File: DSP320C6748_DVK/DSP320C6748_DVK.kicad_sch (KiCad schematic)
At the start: 0 parts

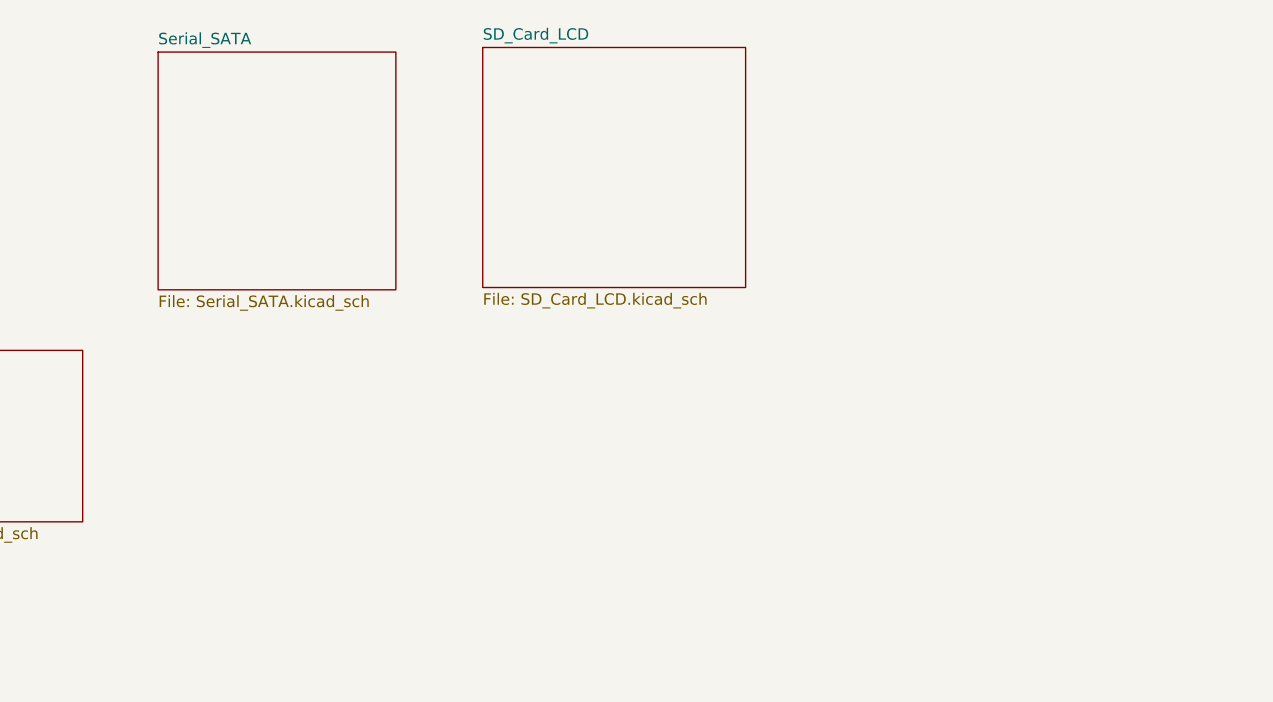
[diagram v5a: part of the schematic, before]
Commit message: DDR_RAM and Video Decoder Schematic Added
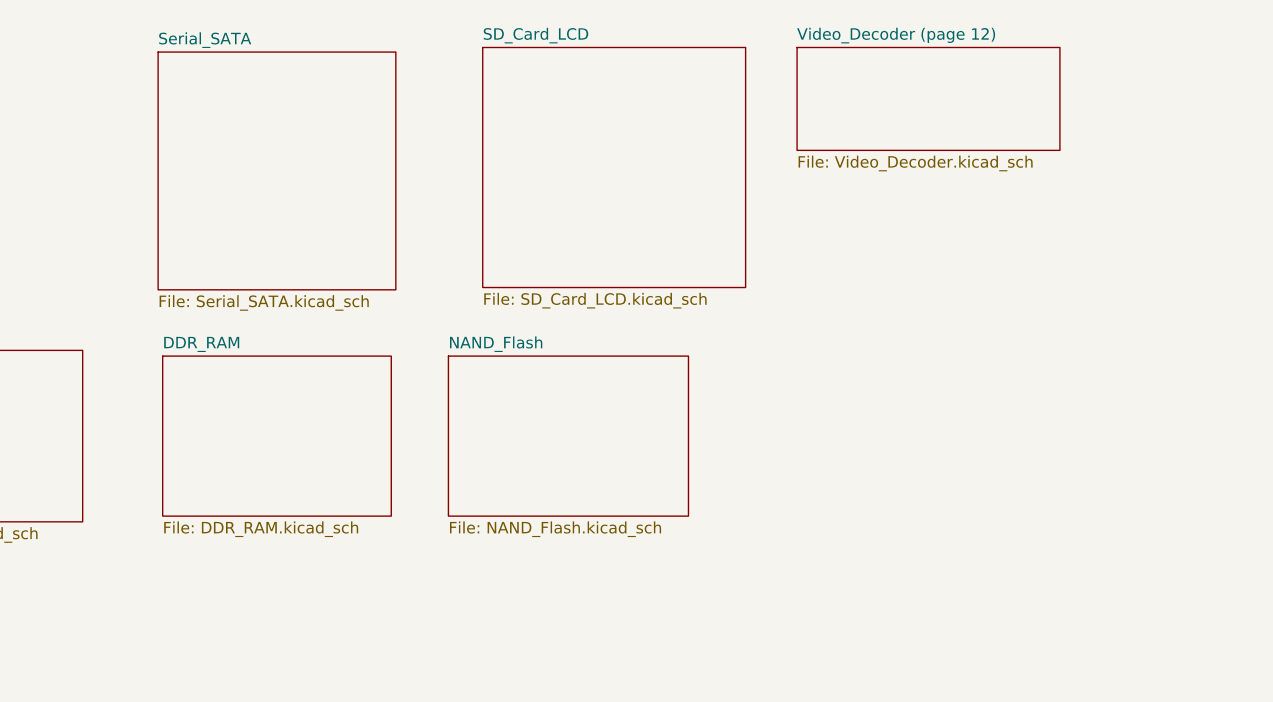
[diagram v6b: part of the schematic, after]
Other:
- added sheet DDR_RAM (DDR_RAM.kicad_sch)
- added sheet NAND_Flash (NAND_Flash.kicad_sch)
- added sheet Video_Decoder (page 12) (Video_Decoder.kicad_sch)
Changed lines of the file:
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@@
+	)
+	(sheet
+		(at 222.885 24.13)
+		(size 29.21 11.43)
+		(exclude_from_sim no)
+		(in_bom yes)
+		(on_board yes)
+		(dnp no)
+		(fields_autoplaced yes)
+		(stroke
+			(width 0.1524)
+			(type solid)
+		)
+		(fill
+			(color 0 0 0 0)
+		)
+		(property "Sheetname" "Video_Decoder (page 12)"
+			(at 222.885 23.4184 0)
+			(show_name no)
+			(do_not_autoplace no)
+			(effects
+				(font
+					(size 1.27 1.27)
+				)
+				(justify left bottom)
+			)
+		)
+		(property "Sheetfile" "Video_Decoder.kicad_sch"
+			(at 222.885 36.1446 0)
+			(show_name no)
+			(do_not_autoplace no)
+			(effects
+				(font
+					(size 1.27 1.27)
+				)
+				(justify left top)
+			)
+		)
+		(instances
+			(project "DSP320C6748_DVK"
+				(path "/3a70ffc0-9fe7-4a5b-b3c2-23140355df82"
+					(page "12")
+				)
+			)
+		)
 	)
 	(sheet
@@
 	)
 	(sheet
+		(at 152.4 58.42)
+		(size 25.4 17.78)
+		(exclude_from_sim no)
+		(in_bom yes)
+		(on_board yes)
+		(dnp no)
+		(fields_autoplaced yes)
+		(stroke
+			(width 0.1524)
+			(type solid)
+		)
+		(fill
+			(color 0 0 0 0)
+		)
+		(property "Sheetname" "DDR_RAM"
+			(at 152.4 57.7084 0)
+			(show_name no)
+			(do_not_autoplace no)
+			(effects
+				(font
+					(size 1.27 1.27)
+				)
+				(justify left bottom)
+			)
+		)
+		(property "Sheetfile" "DDR_RAM.kicad_sch"
+			(at 152.4 76.7846 0)
+			(show_name no)
+			(do_not_autoplace no)
+			(effects
+				(font
+					(size 1.27 1.27)
+				)
+				(justify left top)
+			)
+		)
+		(instances
+			(project "DSP320C6748_DVK"
+				(path "/3a70ffc0-9fe7-4a5b-b3c2-23140355df82"
+					(page "10")
+				)
+			)
+		)
+	)
+	(sheet
 		(at 120.015 57.785)
 		(size 23.495 19.05)
@@
 				)
 			)
+		)
+	)
+	(sheet
+		(at 184.15 58.42)
+		(size 26.67 17.78)
+		(exclude_from_sim no)
+		(in_bom yes)
+		(on_board yes)
+		(dnp no)
+		(fields_autoplaced yes)
+		(stroke
+			(width 0.1524)
+			(type solid)
+		)
+		(fill
+			(color 0 0 0 0)
+		)
+		(property "Sheetname" "NAND_Flash"
+			(at 184.15 57.7084 0)
+			(show_name no)
+			(do_not_autoplace no)
+			(effects
+				(font
+					(size 1.27 1.27)
+				)
+				(justify left bottom)
+			)
+		)
+		(property "Sheetfile" "NAND_Flash.kicad_sch"
+			(at 184.15 76.7846 0)
+			(show_name no)
+			(do_not_autoplace no)
+			(effects
+				(font
+					(size 1.27 1.27)
+				)
+				(justify left top)
+			)
+		)
+		(instances
+			(project "DSP320C6748_DVK"
+				(path "/3a70ffc0-9fe7-4a5b-b3c2-23140355df82"
+					(page "11")
+				)
+			)

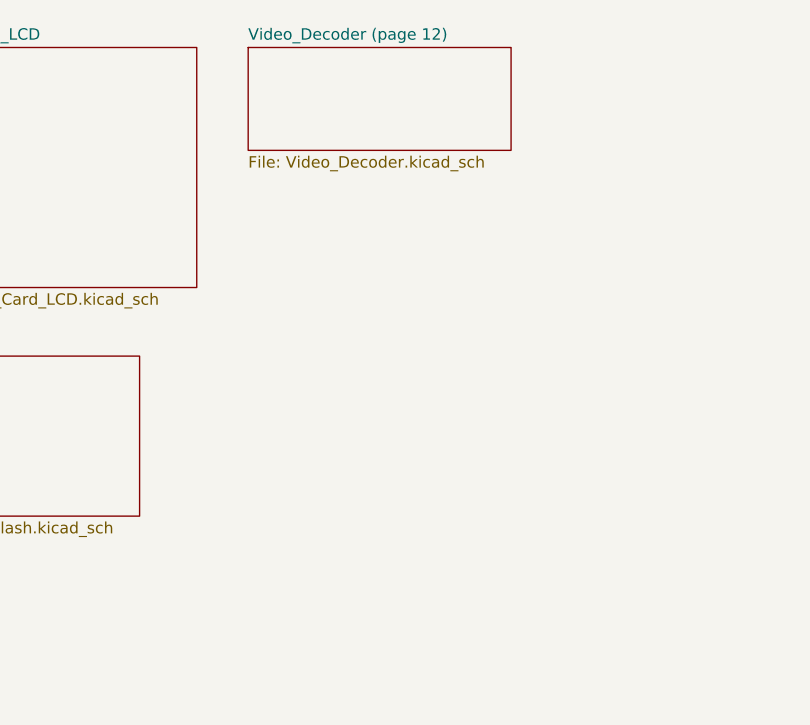
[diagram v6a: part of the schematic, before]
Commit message: Video and Audio Codec Schematic added
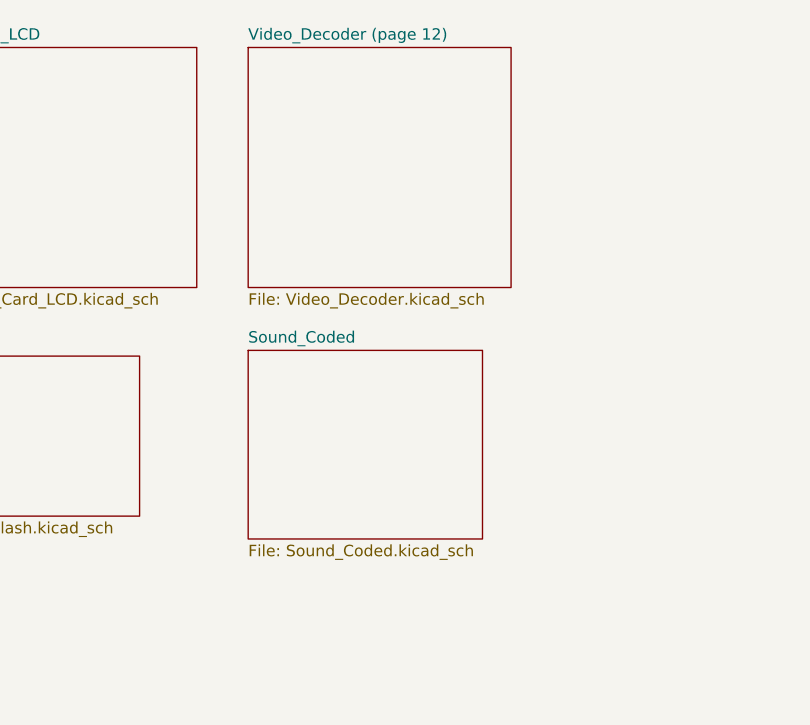
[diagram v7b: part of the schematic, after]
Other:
- added sheet Sound_Coded (Sound_Coded.kicad_sch)
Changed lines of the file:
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@@
 	(sheet
 		(at 222.885 24.13)
-		(size 29.21 11.43)
+		(size 29.21 26.67)
 		(exclude_from_sim no)
 		(in_bom yes)
@@
 		)
 		(property "Sheetfile" "Video_Decoder.kicad_sch"
-			(at 222.885 36.1446 0)
+			(at 222.885 51.3846 0)
 			(show_name no)
 			(do_not_autoplace no)
@@
 				)
 			)
+		)
+	)
+	(sheet
+		(at 222.885 57.785)
+		(size 26.035 20.955)
+		(exclude_from_sim no)
+		(in_bom yes)
+		(on_board yes)
+		(dnp no)
+		(fields_autoplaced yes)
+		(stroke
+			(width 0.1524)
+			(type solid)
+		)
+		(fill
+			(color 0 0 0 0)
+		)
+		(property "Sheetname" "Sound_Coded"
+			(at 222.885 57.0734 0)
+			(show_name no)
+			(do_not_autoplace no)
+			(effects
+				(font
+					(size 1.27 1.27)
+				)
+				(justify left bottom)
+			)
+		)
+		(property "Sheetfile" "Sound_Coded.kicad_sch"
+			(at 222.885 79.3246 0)
+			(show_name no)
+			(do_not_autoplace no)
+			(effects
+				(font
+					(size 1.27 1.27)
+				)
+				(justify left top)
+			)
+		)
+		(instances
+			(project "DSP320C6748_DVK"
+				(path "/3a70ffc0-9fe7-4a5b-b3c2-23140355df82"
+					(page "13")
+				)
+			)

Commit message: LAN Schematic Added
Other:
- added sheet LAN_8710A (LAN_8710A.kicad_sch)
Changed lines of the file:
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@@
+	)
+	(sheet
+		(at 26.035 92.075)
+		(size 34.29 18.415)
+		(exclude_from_sim no)
+		(in_bom yes)
+		(on_board yes)
+		(dnp no)
+		(fields_autoplaced yes)
+		(stroke
+			(width 0.1524)
+			(type solid)
+		)
+		(fill
+			(color 0 0 0 0)
+		)
+		(property "Sheetname" "LAN_8710A"
+			(at 26.035 91.3634 0)
+			(show_name no)
+			(do_not_autoplace no)
+			(effects
+				(font
+					(size 1.27 1.27)
+				)
+				(justify left bottom)
+			)
+		)
+		(property "Sheetfile" "LAN_8710A.kicad_sch"
+			(at 26.035 111.0746 0)
+			(show_name no)
+			(do_not_autoplace no)
+			(effects
+				(font
+					(size 1.27 1.27)
+				)
+				(justify left top)
+			)
+		)
+		(instances
+			(project "DSP320C6748_DVK"
+				(path "/3a70ffc0-9fe7-4a5b-b3c2-23140355df82"
+					(page "14")
+				)
+			)
+		)
 	)
 	(sheet
